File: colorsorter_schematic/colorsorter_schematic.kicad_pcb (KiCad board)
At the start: 2 copper layers, 34 parts, among them J1 Conn_01x03_Pin, J2 Conn_01x03_Pin, J3 Conn_01x03_Pin, J4 Conn_01x05_Pin, J5 Conn_01x06_Pin, J6 Conn_01x03_Pin, J7 Conn_01x03_Pin, J8 Conn_01x02_Pin, SW1 SW_SPDT, U1 PIC24FJ64GA702-I/SO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

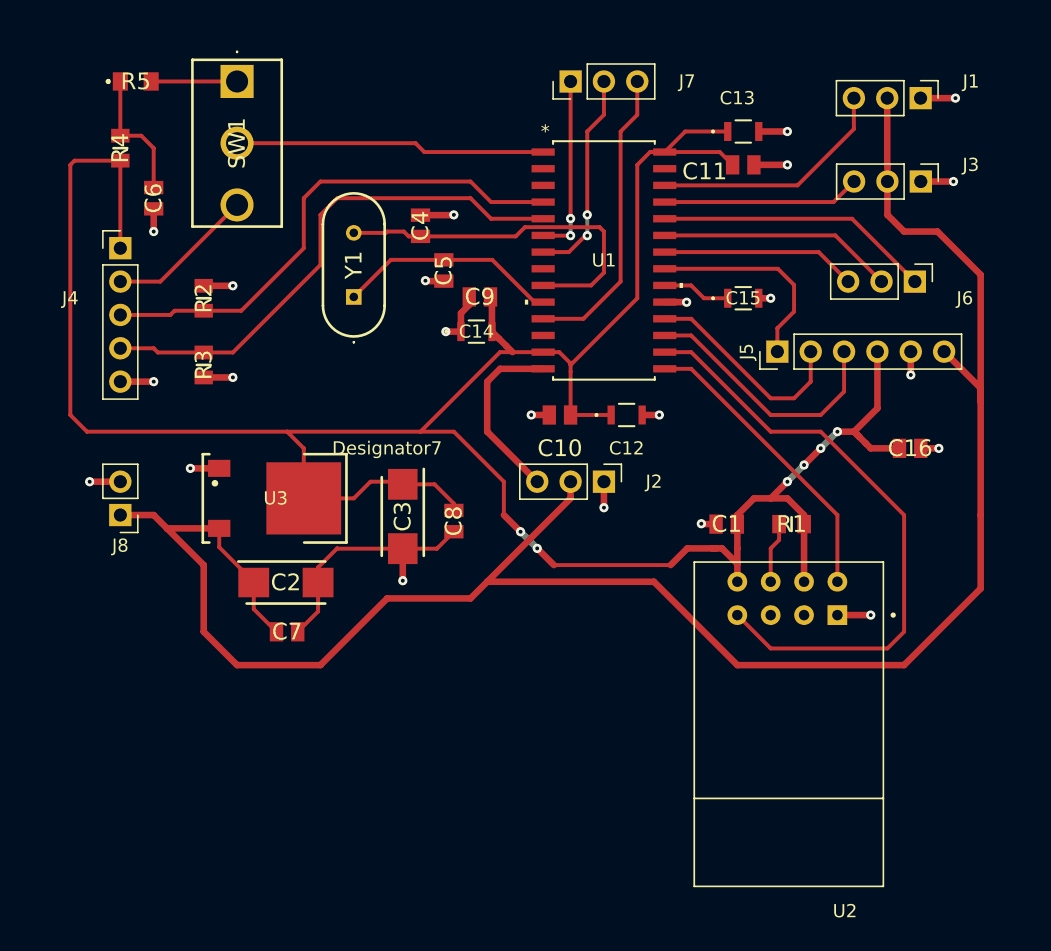
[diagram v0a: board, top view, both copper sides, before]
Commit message: Dodavanje izmjena na pcb fajlu.
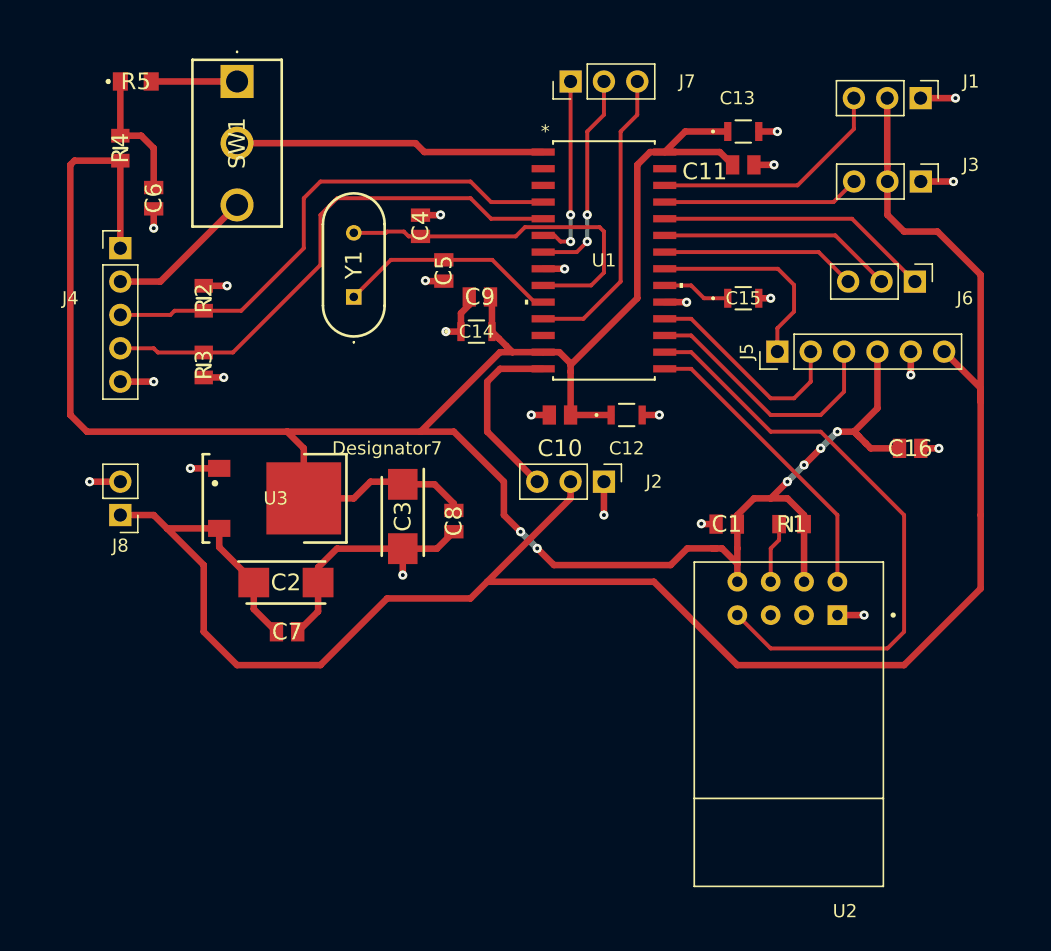
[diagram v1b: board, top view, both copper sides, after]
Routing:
- net GND: track 64.7 -> 61.8 mm, vias 23 -> 24
- net Net-(C3-+): track 199.4 -> 200.2 mm
- net Net-(J7-Pin_1): track 13.8 -> 14.5 mm

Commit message: Final version PCB and manufacturing files
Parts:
- C2, C3: footprint 10uFtantalum:CAPPM6032X280N -> 10uF_tantalum:CAPPM6032X280N
- U3: footprint NDP0003B:NDP0003B -> voltage_regulator:NDP0003B
- renumbered U1 to MCU, Y1 to Oscillator
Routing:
- net GND: track 61.8 -> 64.0 mm, vias 24 -> 25
- added copper zone on B.Cu, net GND
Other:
- board outline added: 76 x 52 mm
- board text added: "ColorSorter_B: Nataša Miljević Ranko Mirosav Danilo Čiča"

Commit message: Added manufaturing and fabrication files
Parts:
- moved R5 0.76 mm to (115.5, 79.9)
- moved SW1 0.63 mm to (123.2, 79.7)
- moved R3 0.25 mm to (120.7, 100.4)
- moved R2 0.25 mm to (120.7, 95.9)
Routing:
- net GND: track 64.0 -> 65.1 mm
- net Net-(C6-Pad2): track 10.1 -> 9.30 mm
- net Net-(C2-+): track 152.2 -> 151.5 mm, vias 0 -> 2
- net Net-(C3-+): vias 6 -> 4
